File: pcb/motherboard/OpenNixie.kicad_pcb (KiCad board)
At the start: 2 copper layers, 229.9 x 64.9 mm, 141 parts, among them J1 Conn_01x02, J10 Conn_01x10, J2 Conn_01x03, J3 Conn_01x03, J4 DC 12V, J5 Conn_01x04, J6 Conn_01x03, J7 Conn_01x10, J8 Conn_01x10, J9 Conn_01x10, Q1 S8050, Q10 MPSA42, Q11 MPSA42, Q12 MPSA42, Q13 MPSA42, Q14 MPSA42, Q15 MPSA42, Q16 MPSA42, Q17 MPSA42, Q18 MPSA42, Q19 MPSA42, Q2 IRFB4620, Q20 MPSA42, Q21 MPSA42, Q22 MPSA42, Q23 MPSA42, Q24 MPSA42, Q25 MPSA42, Q26 MPSA42, Q27 MPSA42, Q28 MPSA42, Q29 MPSA42, Q3 MPSA42, Q30 MPSA42, Q31 MPSA42, Q32 MPSA42, Q33 MPSA42, Q34 MPSA42, Q35 MPSA42, Q36 MPSA42, Q37 MPSA42, Q38 MPSA42, Q39 MPSA42, Q4 MPSA42, Q40 MPSA42, Q41 MPSA42, Q42 MPSA42, Q5 MPSA42, Q6 MPSA42, Q7 MPSA42, Q8 MPSA42, Q9 MPSA42, SW1 SW_SPST, U1 LM7805_TO220, U10 74LS138, U11 74LS138, U12 74LS138, U13 74LS138, U14 74HC595, U15 74LS138, U16 74LS138, U2 NE555P, U3 MAX1771CSA, U4 DS3231M, U5 24LC16, U6 TSDP341xx, U7 74LS138, U8 74LS138, U9 74HC595

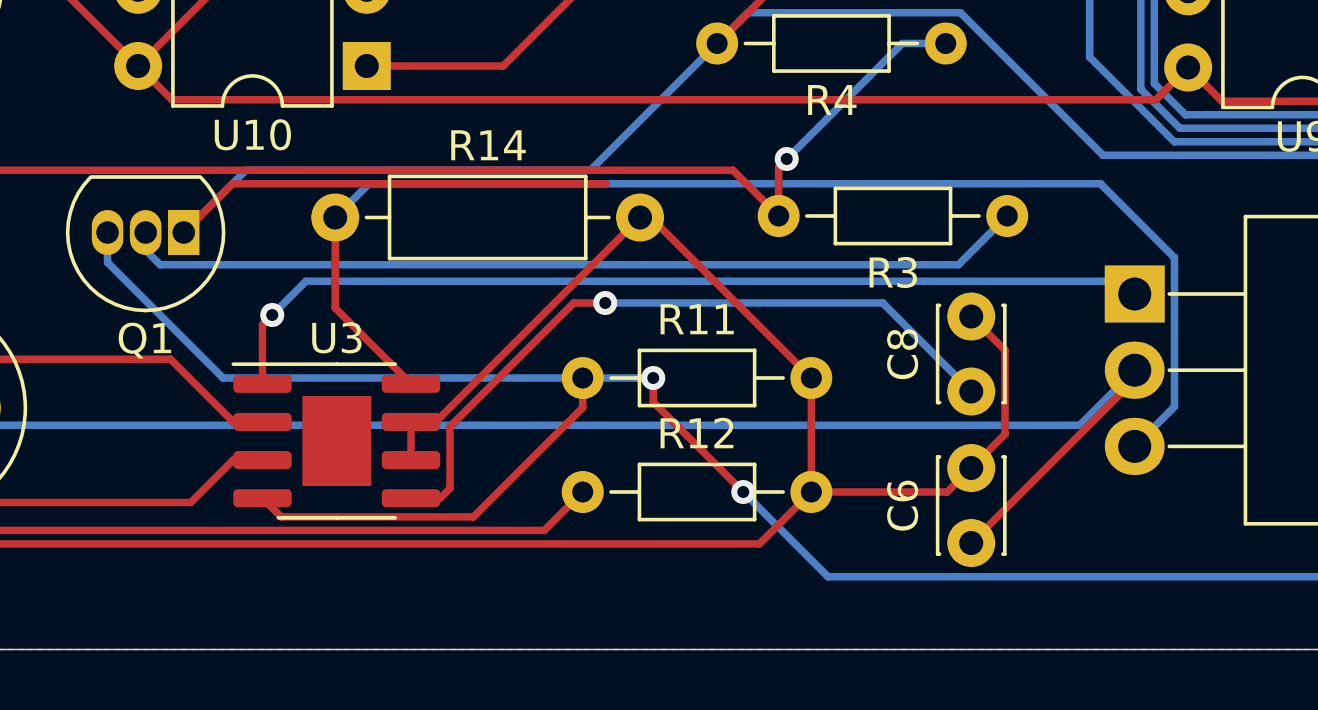
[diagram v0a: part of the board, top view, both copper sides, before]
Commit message: Fix layout errors
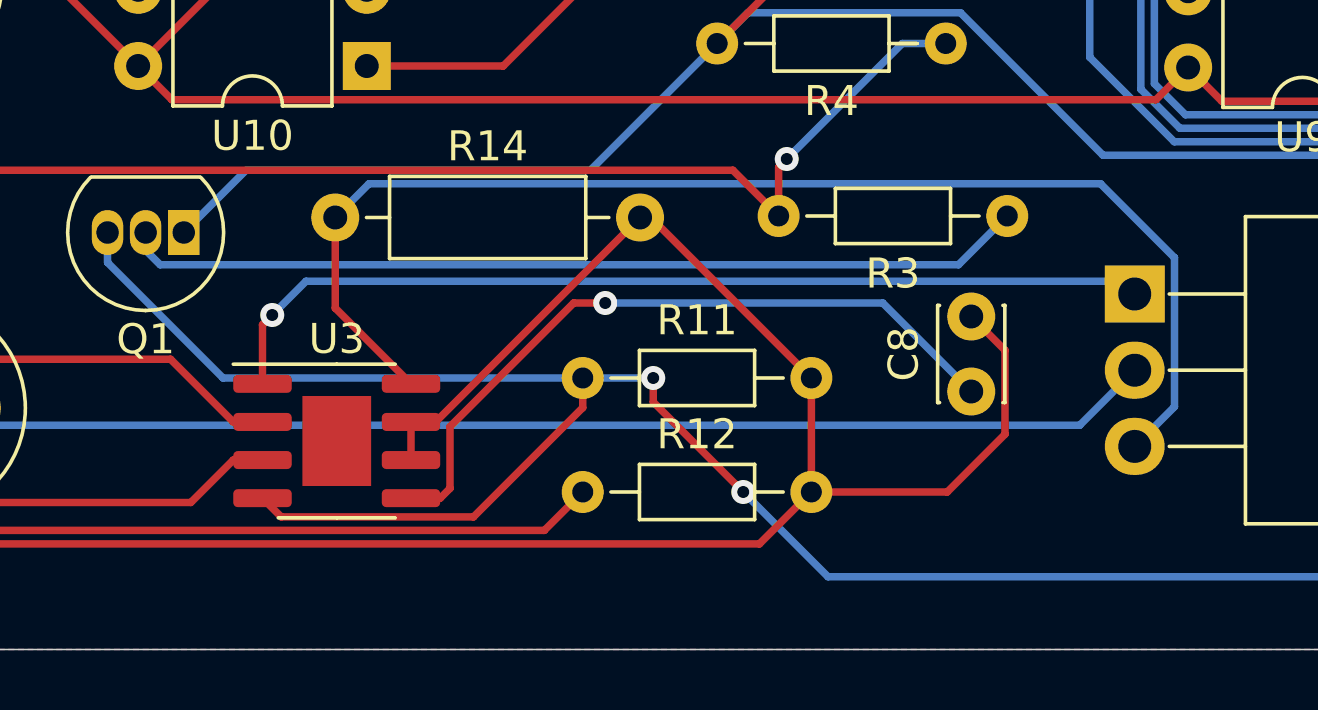
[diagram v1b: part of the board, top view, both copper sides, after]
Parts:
- removed C6: 0.1uF, Capacitor_THT:C_Disc_D3.0mm_W2.0mm_P2.50mm
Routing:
- net GND: track 986.6 -> 971.8 mm
- net Net-(D2-Pad2): track 60.3 -> 52.6 mm

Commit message: Change footprint
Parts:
- C7: footprint Capacitor_THT:CP_Radial_D5.0mm_P2.50mm -> Capacitor_THT:CP_Radial_D8.0mm_P3.80mm
- moved D2 16.2 mm to (142.0, 178.8), turned to 180 degrees
- moved R5 8.36 mm to (126.4, 181.6)
- moved R6 8.36 mm to (126.5, 177.8)
- moved C7 5.69 mm to (112.2, 179.0)
- moved D1 3.35 mm to (118.7, 173.8)
- moved Q1 2.66 mm to (143.3, 172.7)
- moved L1 1.45 mm to (134.7, 177.7), turned to 180 degrees
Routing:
- net GND: track 971.8 -> 933.1 mm
- net Net-(R12-Pad1): track 73.9 -> 58.0 mm
- net Net-(C7-Pad1): track 21.4 -> 36.0 mm
- net BOOST_OUT: track 12.8 -> 21.3 mm
- net Net-(D2-Pad2): track 52.6 -> 57.0 mm
- net Net-(D1-Pad2): track 26.3 -> 22.0 mm
- net Net-(Q1-Pad2): track 30.2 -> 33.0 mm
- net SHDN_PIN: track 92.8 -> 93.4 mm, vias 2 -> 1

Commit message: Fixes
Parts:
- Q2: value IRFB4620 -> TK8P65W; footprint Package_TO_SOT_THT:TO-220-3_Horizontal_TabDown -> Package_TO_SOT_SMD:TO-252-2
- R6: value 20k -> 47k
- moved Q2 9.97 mm to (187.4, 177.3), turned to 0 degrees
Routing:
- net Net-(Q2-Pad3): track 42.9 -> 66.2 mm, vias 0 -> 1
- net Net-(D2-Pad2): track 57.0 -> 68.6 mm, vias 0 -> 1
- net Net-(Q2-Pad1): track 31.8 -> 37.6 mm, vias 1 -> 2

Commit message: Refactoring with 4-bit dynamic scan
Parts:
- removed C1: 10uF, Capacitor_THT:CP_Radial_D5.0mm_P2.50mm
- removed C7: 10uF, Capacitor_THT:CP_Radial_D8.0mm_P3.80mm
- removed C8: 0.1uF, Capacitor_THT:C_Disc_D3.0mm_W2.0mm_P2.50mm
- removed Q18, Q19, Q20, Q21, Q22, Q23, Q24, Q25, Q26, Q27, Q28, Q29, Q30, Q31, Q32, Q33, Q34, Q35, Q36, Q37, Q38, Q39, Q40, Q41, Q42: MPSA42, Package_TO_SOT_THT:TO-92_Inline
- removed R20, R21, R24, R25, R26, R27, R28, R29, R30, R31, R32, R33, R34, R35, R36, R37, R38, R39, R40, R41, R42, R43, R44, R45, R46, R47, R48, R49, R50, R51, R52, R53, R54, R6: 47k, Resistor_THT:R_Axial_DIN0204_L3.6mm_D1.6mm_P7.62mm_Horizontal
- removed R5: 10M, Resistor_THT:R_Axial_DIN0204_L3.6mm_D1.6mm_P7.62mm_Horizontal
- removed REF** (x4): MountingHole_2.1mm, MountingHole:MountingHole_2.1mm
- removed RV1: 200k, Potentiometer_THT:Potentiometer_Vishay_T73YP_Vertical
- removed SW1: SW_SPST, Button_Switch_THT:SW_DIP_SPSTx01_Slide_9.78x4.72mm_W7.62mm_P2.54mm
- removed U11, U12, U13, U15, U16: 74LS138, Package_DIP:DIP-16_W7.62mm
- removed U14: 74HC595, Package_DIP:DIP-16_W7.62mm
- added G1: LOGO, Nixie_Clock:Logo, F.Cu at (166.0, 109.6)
- added J11: Nixie_Conn_12P, Nixie_Clock:Nixie_Conn_12P, F.Cu at (205.9, 96.2)
- added REF1: MountingHole_2.2mm_M2, MountingHole:MountingHole_2.2mm_M2, F.Cu at (77.4, 71.8)
- added REF2: MountingHole_2.2mm_M2, MountingHole:MountingHole_2.2mm_M2, F.Cu at (224.4, 71.8)
- added REF2: MountingHole_2.2mm_M2, MountingHole:MountingHole_2.2mm_M2, F.Cu at (77.4, 121.8)
- added REF3: MountingHole_2.2mm_M2, MountingHole:MountingHole_2.2mm_M2, F.Cu at (224.4, 121.8)
- added locked: 10k, Resistor_THT:R_Axial_DIN0204_L3.6mm_D1.6mm_P2.54mm_Vertical, F.Cu at (127.1, 73.2)
- added locked: 150k, Resistor_THT:R_Axial_DIN0204_L3.6mm_D1.6mm_P2.54mm_Vertical, F.Cu at (127.1, 77.1)
- added locked: 47k, Resistor_THT:R_Axial_DIN0204_L3.6mm_D1.6mm_P2.54mm_Vertical, F.Cu at (107.4, 101.2)
- added locked: 47k, Resistor_THT:R_Axial_DIN0204_L3.6mm_D1.6mm_P2.54mm_Vertical, F.Cu at (135.1, 101.2)
- added locked: 470uF, Capacitor_THT:CP_Radial_D8.0mm_P3.50mm, F.Cu at (107.3, 74.3)
- added locked: 200k, Potentiometer_THT:Potentiometer_Vishay_T73YP_Vertical, F.Cu at (97.0, 73.8)
- BT1: value CR2032 -> 3V; footprint Battery:BatteryHolder_Keystone_1058_1x2032 -> Connector_JST:JST_EH_B2B-EH-A_1x02_P2.50mm_Vertical
- C2: value 1uF -> 10uF; footprint Capacitor_THT:CP_Radial_D5.0mm_P2.50mm -> Capacitor_THT:CP_Radial_D5.0mm_P2.00mm
- C4: value 0.1uF -> 10uF; footprint Capacitor_THT:C_Disc_D3.0mm_W2.0mm_P2.50mm -> Capacitor_THT:CP_Radial_D8.0mm_P3.80mm
- C5: value 470uF -> 0.1uF; footprint Capacitor_THT:CP_Radial_D8.0mm_P3.50mm -> Capacitor_THT:C_Disc_D3.0mm_W2.0mm_P2.50mm
- D1: footprint Diode_THT:D_DO-35_SOD27_P7.62mm_Horizontal -> Diode_THT:D_DO-35_SOD27_P2.54mm_Vertical_AnodeUp
- D3: value LED_RCGB -> LED_RKGB; footprint LED_THT:LED_D5.0mm-4_RGB -> LED_THT:LED_D5.0mm-4_RGB_Wide_Pins
- J10, J8, J9: value Conn_01x10 -> Nixie_Conn_12P; footprint Connector_JST:JST_EH_B10B-EH-A_1x10_P2.50mm_Vertical -> Nixie_Clock:Nixie_Conn_12P
- J2: value Conn_01x03 -> Conn_01x02; footprint Connector_JST:JST_EH_B3B-EH-A_1x03_P2.50mm_Vertical -> Connector_JST:JST_EH_B2B-EH-A_1x02_P2.50mm_Vertical
- J4: value DC 12V -> Nixie_Conn_4P; footprint Connector_BarrelJack:BarrelJack_Horizontal -> Nixie_Clock:Nixie_Conn_4P
- J6: value Conn_01x03 -> 12V; footprint Connector_JST:JST_EH_B3B-EH-A_1x03_P2.50mm_Vertical -> Connector_BarrelJack:BarrelJack_Horizontal
- J7: value Conn_01x10 -> Conn_01x03; footprint Connector_JST:JST_EH_B10B-EH-A_1x10_P2.50mm_Vertical -> Connector_JST:JST_EH_B3B-EH-A_1x03_P2.50mm_Vertical
- Q1: value S8050 -> MPSA42
- Q2: value TK8P65W -> MPSA42; footprint Package_TO_SOT_SMD:TO-252-2 -> Package_TO_SOT_THT:TO-92_Inline
- Q3: value MPSA42 -> TK8P65W; footprint Package_TO_SOT_THT:TO-92_Inline -> Package_TO_SOT_SMD:TO-252-2
- R1, R3: value 1k -> 150k; footprint Resistor_THT:R_Axial_DIN0204_L3.6mm_D1.6mm_P7.62mm_Horizontal -> Resistor_THT:R_Axial_DIN0204_L3.6mm_D1.6mm_P2.54mm_Vertical
- R10, R11, R9: value 4.7k -> 10k; footprint Resistor_THT:R_Axial_DIN0204_L3.6mm_D1.6mm_P7.62mm_Horizontal -> Resistor_THT:R_Axial_DIN0204_L3.6mm_D1.6mm_P2.54mm_Vertical
- R12: value 68k -> 10k; footprint Resistor_THT:R_Axial_DIN0204_L3.6mm_D1.6mm_P7.62mm_Horizontal -> Resistor_THT:R_Axial_DIN0204_L3.6mm_D1.6mm_P2.54mm_Vertical
- R13: value 500 -> 68k; footprint Resistor_THT:R_Axial_DIN0204_L3.6mm_D1.6mm_P7.62mm_Horizontal -> Resistor_THT:R_Axial_DIN0204_L3.6mm_D1.6mm_P2.54mm_Vertical
- R15: value 47k -> 1k; footprint Resistor_THT:R_Axial_DIN0204_L3.6mm_D1.6mm_P7.62mm_Horizontal -> Resistor_THT:R_Axial_DIN0204_L3.6mm_D1.6mm_P2.54mm_Vertical
- R16, R17, R18, R19, R22, R23: footprint Resistor_THT:R_Axial_DIN0204_L3.6mm_D1.6mm_P7.62mm_Horizontal -> Resistor_THT:R_Axial_DIN0204_L3.6mm_D1.6mm_P2.54mm_Vertical
- R2: value 100k -> 1k; footprint Resistor_THT:R_Axial_DIN0204_L3.6mm_D1.6mm_P7.62mm_Horizontal -> Resistor_THT:R_Axial_DIN0204_L3.6mm_D1.6mm_P2.54mm_Vertical
- R4: value 1M -> 10k; footprint Resistor_THT:R_Axial_DIN0204_L3.6mm_D1.6mm_P7.62mm_Horizontal -> Resistor_THT:R_Axial_DIN0204_L3.6mm_D1.6mm_P2.54mm_Vertical
- R7: value 10k -> 150k; footprint Resistor_THT:R_Axial_DIN0204_L3.6mm_D1.6mm_P7.62mm_Horizontal -> Resistor_THT:R_Axial_DIN0204_L3.6mm_D1.6mm_P2.54mm_Vertical
- R8: value 10k -> 10M; footprint Resistor_THT:R_Axial_DIN0204_L3.6mm_D1.6mm_P7.62mm_Horizontal -> Resistor_THT:R_Axial_DIN0204_L3.6mm_D1.6mm_P2.54mm_Vertical
- U10: value 74LS138 -> 74HC04; footprint Package_DIP:DIP-16_W7.62mm -> Package_DIP:DIP-14_W7.62mm
- U3: value MAX1771CSA -> NE555P; footprint Package_SO:SOIC-8-1EP_3.9x4.9mm_P1.27mm_EP2.29x3mm -> Package_DIP:DIP-8_W7.62mm
- U4: value DS3231M -> MAX1771CSA; footprint Package_SO:SOIC-16W_7.5x10.3mm_P1.27mm -> Package_SO:SO-8_3.9x4.9mm_P1.27mm
- U5: value 24LC16 -> DS3231M; footprint Package_DIP:DIP-8_W7.62mm -> Package_SO:SOIC-16W_7.5x10.3mm_P1.27mm
- U6: value TSDP341xx -> 74LS138; footprint OptoDevice:Vishay_MOLD-3Pin -> Package_DIP:DIP-16_W7.62mm
- U7: value 74LS138 -> 74HC595
- U9: value 74HC595 -> 74HC04; footprint Package_DIP:DIP-16_W7.62mm -> Package_DIP:DIP-14_W7.62mm
- moved J2 207.6 mm to (126.0, 85.8), turned to 90 degrees
- moved U6 196.7 mm to (110.4, 113.4), turned to -90 degrees
- moved U5 192.5 mm to (99.9, 83.7), turned to 180 degrees
- moved J6 189.5 mm to (150.9, 83.3), turned to -90 degrees
- moved BT1 165.9 mm to (90.3, 76.0)
- moved J3 162.3 mm to (159.2, 119.5)
- moved U8 160.4 mm to (78.6, 77.7), turned to 0 degrees
- moved R10 150.2 mm to (90.4, 85.7)
- moved R9 144.4 mm to (90.4, 80.7), turned to -90 degrees
- moved R13 143.9 mm to (141.4, 87.5), turned to 0 degrees
- moved R1 136.3 mm to (132.7, 73.2)
- moved U4 133.2 mm to (142.0, 95.8)
- moved Q2 125.0 mm to (115.6, 75.0)
- moved L1 116.7 mm to (193.0, 76.6)
- moved C3 110.5 mm to (200.7, 76.6), turned to 0 degrees
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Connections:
- BT1 pad 1: Net-(BT1-Pad1) -> Net-(#FLG03-pwr)
- C2 pad 1: +12V -> Net-(U2-THR)
- C3 pad 1: Net-(C3-Pad1) -> +12V
- C4 pad 1: +5V -> Net-(D2-K)
- C5 pad 1: +12V -> GND
- C5 pad 2: GND -> Net-(U4-REF)
- D1 pad 1: CONSTANT_PIN -> SHDN_PIN
- D1 pad 2: Net-(D1-Pad2) -> Net-(D1-A)
- D2 pad 1: Net-(C7-Pad1) -> Net-(D2-K)
- D2 pad 2: Net-(D2-Pad2) -> Net-(D2-A)
- D3 pad 1: RED_PIN -> RGB_RED
- D3 pad 2: Net-(D3-Pad2) -> Net-(D3-K)
- D3 pad 3: GREEN_PIN -> RGB_GRN
- D3 pad 4: BLUE_PIN -> RGB_BLE
- J1 pad 1: TIMER_PIN -> I2C_SCL
- J1 pad 2: CONSTANT_PIN -> I2C_SDA
- J10 pad 1: NIXIE_3_P0 -> /NIXIE_Y_P1
- J10 pad 10: NIXIE_3_P9 -> unconnected-(J10-Pad10)
- J10 pad 2: NIXIE_3_P1 -> /NIXIE_Y_P2
- J10 pad 3: NIXIE_3_P2 -> /NIXIE_Y_P3
- J10 pad 4: NIXIE_3_P3 -> /NIXIE_Y_P4
- J10 pad 5: NIXIE_3_P4 -> /NIXIE_Y_P5
- J10 pad 6: NIXIE_3_P5 -> /NIXIE_Y_P6
- J10 pad 7: NIXIE_3_P6 -> /NIXIE_Y_P7
- J10 pad 8: NIXIE_3_P7 -> /NIXIE_Y_P8
- J10 pad 9: NIXIE_3_P8 -> /NIXIE_Y_P9
- J2 pad 1: RED_PIN -> LIGHT_PIN
- J2 pad 2: GREEN_PIN -> SHDN_PIN
- J3 pad 1: LATCH_PIN -> SR_LATCH
- J3 pad 2: DATA_PIN -> SR_DATA
- J3 pad 3: CLOCK_PIN -> SR_CLK
- J5 pad 3: BOOST_OUT -> +170V
- J6 pad 1: I2C_SCL -> +12V
- J6 pad 2: I2C_SDA -> GND
- J6 pad 3: IR_OUT -> unconnected-(J6-Pad3)
- J7 pad 1: NIXIE_0_P0 -> RGB_RED
- J7 pad 2: NIXIE_0_P1 -> RGB_GRN
- J7 pad 3: NIXIE_0_P2 -> RGB_BLE
- J8 pad 1: NIXIE_1_P0 -> /NIXIE_Y_P1
- J8 pad 10: NIXIE_1_P9 -> unconnected-(J8-Pad10)
- J8 pad 2: NIXIE_1_P1 -> /NIXIE_Y_P2
- J8 pad 3: NIXIE_1_P2 -> /NIXIE_Y_P3
- J8 pad 4: NIXIE_1_P3 -> /NIXIE_Y_P4
- J8 pad 5: NIXIE_1_P4 -> /NIXIE_Y_P5
- J8 pad 6: NIXIE_1_P5 -> /NIXIE_Y_P6
- J8 pad 7: NIXIE_1_P6 -> /NIXIE_Y_P7
- J8 pad 8: NIXIE_1_P7 -> /NIXIE_Y_P8
- J8 pad 9: NIXIE_1_P8 -> /NIXIE_Y_P9
- J9 pad 1: NIXIE_2_P0 -> /NIXIE_Y_P1
- J9 pad 10: NIXIE_2_P9 -> unconnected-(J9-Pad10)
- J9 pad 2: NIXIE_2_P1 -> /NIXIE_Y_P2
- J9 pad 3: NIXIE_2_P2 -> /NIXIE_Y_P3
- J9 pad 4: NIXIE_2_P3 -> /NIXIE_Y_P4
- J9 pad 5: NIXIE_2_P4 -> /NIXIE_Y_P5
- J9 pad 6: NIXIE_2_P5 -> /NIXIE_Y_P6
- J9 pad 7: NIXIE_2_P6 -> /NIXIE_Y_P7
- J9 pad 8: NIXIE_2_P7 -> /NIXIE_Y_P8
- J9 pad 9: NIXIE_2_P8 -> /NIXIE_Y_P9
- L1 pad 1: +12V -> Net-(D2-A)
- L1 pad 2: Net-(D2-Pad2) -> +12V
- Q1 pad 2: Net-(Q1-Pad2) -> Net-(Q1-B)
- Q1 pad 3: SHDN_PIN -> Net-(Q1-C)
- Q10 pad 2: Net-(Q10-Pad2) -> /NPN_Y_P2
- Q10 pad 3: NIXIE_1_P2 -> /NIXIE_Y_P2
- Q11 pad 2: Net-(Q11-Pad2) -> /NPN_Y_P3
- Q11 pad 3: NIXIE_0_P5 -> /NIXIE_Y_P3
- Q12 pad 2: Net-(Q12-Pad2) -> /NPN_Y_P4
- Q12 pad 3: NIXIE_1_P5 -> /NIXIE_Y_P4
- Q13 pad 2: Net-(Q13-Pad2) -> /NPN_Y_P5
- Q13 pad 3: NIXIE_0_P4 -> /NIXIE_Y_P5
- Q14 pad 2: Net-(Q14-Pad2) -> /NPN_Y_P6
- Q14 pad 3: NIXIE_1_P4 -> /NIXIE_Y_P6
- Q15 pad 2: Net-(Q15-Pad2) -> /NPN_Y_P7
- Q15 pad 3: NIXIE_0_P7 -> /NIXIE_Y_P7
- Q16 pad 2: Net-(Q16-Pad2) -> /NPN_Y_P8
- Q16 pad 3: NIXIE_1_P7 -> /NIXIE_Y_P8
- Q17 pad 2: Net-(Q17-Pad2) -> /NPN_Y_P9
- Q17 pad 3: NIXIE_0_P6 -> /NIXIE_Y_P9
- Q2 pad 1: Net-(Q2-Pad1) -> GND
- Q2 pad 2: Net-(D2-Pad2) -> Net-(Q2-B)
- Q2 pad 3: Net-(Q2-Pad3) -> Net-(D1-A)
- Q3 pad 1: GND -> Net-(Q3-G)
- Q3 pad 2: Net-(Q3-Pad2) -> Net-(D2-A)
- Q3 pad 3: NIXIE_0_P1 -> Net-(Q3-S)
- Q4 pad 2: Net-(Q4-Pad2) -> Net-(Q4-B)
- Q4 pad 3: NIXIE_1_P1 -> /NIXIE_X_P0
- Q5 pad 2: Net-(Q5-Pad2) -> Net-(Q5-B)
- Q5 pad 3: NIXIE_0_P0 -> /NIXIE_X_P1
- Q6 pad 2: Net-(Q6-Pad2) -> Net-(Q6-B)
- Q6 pad 3: NIXIE_1_P0 -> /NIXIE_X_P2
- Q7 pad 2: Net-(Q7-Pad2) -> Net-(Q7-B)
- Q7 pad 3: NIXIE_0_P3 -> /NIXIE_X_P3
- Q8 pad 2: Net-(Q8-Pad2) -> /NPN_Y_P0
- Q8 pad 3: NIXIE_1_P3 -> /NIXIE_Y_P0
- Q9 pad 2: Net-(Q9-Pad2) -> /NPN_Y_P1
- Q9 pad 3: NIXIE_0_P2 -> /NIXIE_Y_P1
- R1 pad 1: SHDN_PIN -> Net-(D1-A)
- R10 pad 2: I2C_SDA -> I2C_SCL
- R12 pad 1: Net-(R12-Pad1) -> Net-(D2-K)
- R12 pad 2: GND -> +170V
- R13 pad 1: Net-(D3-Pad2) -> GND
- R13 pad 2: GND -> Net-(U4-FB)
- R14 pad 1: Net-(Q2-Pad3) -> GND
- R14 pad 2: GND -> Net-(Q3-S)
- R15 pad 1: Net-(Q3-Pad2) -> GND
- R15 pad 2: /138_0_P1 -> Net-(D3-K)
- R16 pad 1: Net-(Q4-Pad2) -> +170V
- R16 pad 2: /138_1_P1 -> /NIXIE_X_P1
- R17 pad 1: Net-(Q5-Pad2) -> +170V
- R17 pad 2: /138_0_P0 -> /NIXIE_X_P3
- R18 pad 1: Net-(Q6-Pad2) -> +170V
- R18 pad 2: /138_1_P0 -> /NIXIE_X_P0
- R19 pad 1: Net-(Q7-Pad2) -> +170V
- R19 pad 2: /138_0_P3 -> /NIXIE_X_P2
- R2 pad 1: TIMER_PIN -> Net-(U2-DIS)
- R22 pad 1: Net-(Q10-Pad2) -> /NPN_X_P2
- R22 pad 2: /138_1_P2 -> Net-(Q6-B)
- R23 pad 1: Net-(Q11-Pad2) -> /NPN_X_P3
- R23 pad 2: /138_0_P5 -> Net-(Q7-B)
- R3 pad 1: Net-(Q1-Pad2) -> Net-(J4-PadGND)
- R3 pad 2: CONSTANT_PIN -> Net-(Q1-C)
- R4 pad 1: CONSTANT_PIN -> Net-(U2-Q)
- R4 pad 2: GND -> Net-(Q1-B)
- R7 pad 1: +5V -> Net-(U2-THR)
- R7 pad 2: I2C_SDA -> Net-(U2-DIS)
- R8 pad 1: +5V -> Net-(D2-K)
- R8 pad 2: I2C_SCL -> Net-(U4-FB)
- R9 pad 2: I2C_SCL -> I2C_SDA
- U10 pad 1: /595_0_P0 -> /Decoder Inverter/IN_P6
- U10 pad 10: (no net) -> unconnected-(U10-Pad10)
- U10 pad 11: (no net) -> unconnected-(U10-Pad11)
- U10 pad 12: (no net) -> unconnected-(U10-Pad12)
- U10 pad 13: (no net) -> unconnected-(U10-Pad13)
- U10 pad 14: Net-(R29-Pad2) -> +5V
- U10 pad 2: /595_0_P1 -> /NPN_Y_P6
- U10 pad 3: /595_0_P2 -> /Decoder Inverter/IN_P7
- U10 pad 4: GND -> /NPN_Y_P7
- U10 pad 5: GND -> /Decoder Inverter/IN_P8
- U10 pad 6: /595_0_P3 -> /NPN_Y_P8
- U10 pad 7: (no net) -> GND
- U10 pad 8: GND -> /NPN_Y_P9
- U10 pad 9: (no net) -> /Decoder Inverter/IN_P9
- U2 pad 2: TIMER_PIN -> Net-(U2-THR)
- U2 pad 3: Net-(D1-Pad2) -> Net-(U2-Q)
- U2 pad 5: (no net) -> unconnected-(U2-CV-Pad5)
- U2 pad 6: Net-(C3-Pad1) -> Net-(U2-THR)
- U2 pad 7: Net-(C3-Pad1) -> Net-(U2-DIS)
- U3 pad 1: Net-(Q2-Pad1) -> GND
- U3 pad 2: +12V -> LIGHT_PIN
- U3 pad 3: Net-(R12-Pad1) -> Net-(U3-Q)
- U3 pad 4: SHDN_PIN -> +5V
- U3 pad 5: Net-(C8-Pad1) -> unconnected-(U3-CV-Pad5)
- U3 pad 6: GND -> Net-(U3-DIS)
- U3 pad 7: GND -> Net-(U3-DIS)
- U3 pad 8: Net-(Q2-Pad3) -> +5V
- U4 pad 1: (no net) -> Net-(Q3-G)
- U4 pad 2: +5V -> +12V
- U4 pad 3: (no net) -> Net-(U4-FB)
- U4 pad 4: (no net) -> SHDN_PIN
- U4 pad 5: GND -> Net-(U4-REF)
- U4 pad 8: GND -> Net-(Q3-S)
- U5 pad 1: GND -> unconnected-(U5-32KHZ-Pad1)
- U5 pad 2: GND -> +5V
- U5 pad 3: GND -> unconnected-(U5-~{INT}/SQW-Pad3)
- U5 pad 4: GND -> unconnected-(U5-~{RST}-Pad4)
- U5 pad 5: I2C_SDA -> GND
- U5 pad 6: I2C_SCL -> GND
- U5 pad 8: +5V -> GND
- U6 pad 1: IR_OUT -> /DECODER_P0
- U6 pad 2: GND -> /DECODER_P1
- U6 pad 3: +5V -> /DECODER_P2
- U7 pad 1: /595_0_P0 -> /DECODER_P1
- U7 pad 10: /138_0_P5 -> +5V
- U7 pad 11: /138_0_P4 -> SR_CLK
- U7 pad 12: /138_0_P3 -> SR_LATCH
- U7 pad 13: /138_0_P2 -> GND
- U7 pad 14: /138_0_P1 -> SR_DATA
- U7 pad 15: /138_0_P0 -> /DECODER_P0
- U7 pad 2: /595_0_P1 -> /DECODER_P2
- U7 pad 3: /595_0_P2 -> /DECODER_P3
- U7 pad 4: /595_0_P3 -> /NPN_X_P0
- U7 pad 5: GND -> /NPN_X_P1
- U7 pad 6: +5V -> /NPN_X_P2
- U7 pad 7: /138_0_P7 -> /NPN_X_P3
- U7 pad 9: /138_0_P6 -> unconnected-(U7-QH'-Pad9)
- U8 pad 1: /595_0_P4 -> /DECODER_P0
- U8 pad 10: /138_1_P5 -> unconnected-(U8-O5-Pad10)
- U8 pad 11: /138_1_P4 -> unconnected-(U8-O4-Pad11)
- U8 pad 12: /138_1_P3 -> unconnected-(U8-O3-Pad12)
- U8 pad 13: /138_1_P2 -> unconnected-(U8-O2-Pad13)
- U8 pad 14: /138_1_P1 -> /Decoder Inverter/IN_P9
- U8 pad 15: /138_1_P0 -> /Decoder Inverter/IN_P8
- U8 pad 2: /595_0_P5 -> /DECODER_P1
- U8 pad 3: /595_0_P6 -> /DECODER_P2
- U8 pad 4: /595_0_P7 -> GND
- U8 pad 6: +5V -> /DECODER_P3
- U8 pad 7: /138_1_P7 -> unconnected-(U8-O7-Pad7)
- U8 pad 9: /138_1_P6 -> unconnected-(U8-O6-Pad9)
- U9 pad 1: /595_0_P1 -> /Decoder Inverter/IN_P0
- U9 pad 10: +5V -> /NPN_Y_P4
- U9 pad 11: CLOCK_PIN -> /Decoder Inverter/IN_P4
- U9 pad 12: LATCH_PIN -> /NPN_Y_P5
- U9 pad 13: GND -> /Decoder Inverter/IN_P5
- U9 pad 14: DATA_PIN -> +5V
- U9 pad 2: /595_0_P2 -> /NPN_Y_P0
- U9 pad 3: /595_0_P3 -> /Decoder Inverter/IN_P1
- U9 pad 4: /595_0_P4 -> /NPN_Y_P1
- U9 pad 5: /595_0_P5 -> /Decoder Inverter/IN_P2
- U9 pad 6: /595_0_P6 -> /NPN_Y_P2
- U9 pad 7: /595_0_P7 -> GND
- U9 pad 8: GND -> /NPN_Y_P3
- U9 pad 9: CASCADE_PIN -> /Decoder Inverter/IN_P3
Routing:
- net GND: track 933.1 -> 0.00 mm, vias 2 -> 0
- net +5V: track 637.0 -> 300.2 mm
- net +170V: track 0.00 -> 217.3 mm, vias 0 -> 1
- net /NIXIE_Y_P3: track 0.00 -> 182.1 mm
- net /NIXIE_Y_P1: track 0.00 -> 178.1 mm
- net /NIXIE_Y_P5: track 0.00 -> 176.3 mm
- net CLOCK_PIN: track 175.8 -> 0.00 mm, vias 1 -> 0
- net /NIXIE_Y_P2: track 0.00 -> 170.5 mm
- net /NIXIE_Y_P4: track 0.00 -> 169.2 mm
- net /NIXIE_Y_P6: track 0.00 -> 164.8 mm
- net LATCH_PIN: track 160.0 -> 0.00 mm, vias 3 -> 0
- net /NIXIE_Y_P7: track 0.00 -> 158.4 mm
- net /NIXIE_Y_P0: track 0.00 -> 154.3 mm
- net /NIXIE_Y_P9: track 0.00 -> 153.3 mm
- net /NIXIE_Y_P8: track 0.00 -> 152.7 mm
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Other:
- board size 229.9 x 64.9 mm -> 152 x 55 mm
- net class Default removed
- board text added: "OpenNixie@ibcl.us https://github.com/bclswl0827/OpenNixie"

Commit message: Ver 3.0
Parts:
- removed BT1: 3V, Connector_JST:JST_EH_B2B-EH-A_1x02_P2.50mm_Vertical
- removed the J1 at (108.9, 85.9)
- removed the R10 at (90.4, 85.7)
- removed R22, R23: 47k, Resistor_THT:R_Axial_DIN0204_L3.6mm_D1.6mm_P2.54mm_Vertical
- removed the R9 at (90.4, 80.7)
- removed the REF2 at (77.4, 121.8)
- removed the U5 at (99.9, 83.7)
- removed the U9 at (130.4, 113.4)
- removed the locked at (107.4, 101.2)
- removed the locked at (135.1, 101.2)
- added Q10: S8050, Package_TO_SOT_THT:TO-92_Inline, F.Cu at (164.9, 108.9)
- added Q11: S8050, Package_TO_SOT_THT:TO-92_Inline, F.Cu at (158.6, 108.8)
- added Q8: S8050, Package_TO_SOT_THT:TO-92_Inline, F.Cu at (177.2, 108.8)
- added Q9: S8050, Package_TO_SOT_THT:TO-92_Inline, F.Cu at (171.0, 108.9)
- added R18: 47k, Resistor_THT:R_Axial_DIN0204_L3.6mm_D1.6mm_P5.08mm_Horizontal, F.Cu at (138.6, 94.4)
- added R19: 47k, Resistor_THT:R_Axial_DIN0204_L3.6mm_D1.6mm_P5.08mm_Horizontal, F.Cu at (192.8, 94.4)
- added R20: 47k, Resistor_THT:R_Axial_DIN0204_L3.6mm_D1.6mm_P5.08mm_Horizontal, F.Cu at (110.6, 94.4)
- added R21: 47k, Resistor_THT:R_Axial_DIN0204_L3.6mm_D1.6mm_P5.08mm_Horizontal, F.Cu at (165.2, 94.4)
- added REF4: MountingHole_2.2mm_M2, MountingHole:MountingHole_2.2mm_M2, F.Cu at (77.4, 121.8)
- added U8: 74HC04, Package_DIP:DIP-14_W7.62mm, F.Cu at (130.4, 113.4)
- Q2: value MPSA42 -> S8050
- R1: value 150k -> 47k; footprint Resistor_THT:R_Axial_DIN0204_L3.6mm_D1.6mm_P2.54mm_Vertical -> Resistor_THT:R_Axial_DIN0204_L3.6mm_D1.6mm_P5.08mm_Horizontal
- R10: renamed from R12; value 10k -> 6.8k; footprint Resistor_THT:R_Axial_DIN0204_L3.6mm_D1.6mm_P2.54mm_Vertical -> Resistor_THT:R_Axial_DIN0309_L9.0mm_D3.2mm_P12.70mm_Horizontal
- R11: renamed from R13; footprint Resistor_THT:R_Axial_DIN0204_L3.6mm_D1.6mm_P2.54mm_Vertical -> Resistor_THT:R_Axial_DIN0204_L3.6mm_D1.6mm_P5.08mm_Horizontal
- R12: renamed from R15; footprint Resistor_THT:R_Axial_DIN0204_L3.6mm_D1.6mm_P2.54mm_Vertical -> Resistor_THT:R_Axial_DIN0204_L3.6mm_D1.6mm_P5.08mm_Horizontal
- R14: renamed from R16; footprint Resistor_THT:R_Axial_DIN0204_L3.6mm_D1.6mm_P2.54mm_Vertical -> Resistor_THT:R_Axial_DIN0309_L9.0mm_D3.2mm_P12.70mm_Horizontal
- R15: renamed from R17; footprint Resistor_THT:R_Axial_DIN0204_L3.6mm_D1.6mm_P2.54mm_Vertical -> Resistor_THT:R_Axial_DIN0309_L9.0mm_D3.2mm_P12.70mm_Horizontal
- R16: renamed from R18; footprint Resistor_THT:R_Axial_DIN0204_L3.6mm_D1.6mm_P2.54mm_Vertical -> Resistor_THT:R_Axial_DIN0309_L9.0mm_D3.2mm_P12.70mm_Horizontal
- R17: renamed from R19; footprint Resistor_THT:R_Axial_DIN0204_L3.6mm_D1.6mm_P2.54mm_Vertical -> Resistor_THT:R_Axial_DIN0309_L9.0mm_D3.2mm_P12.70mm_Horizontal
- R2, R4, R7, R8, locked (x2): footprint Resistor_THT:R_Axial_DIN0204_L3.6mm_D1.6mm_P2.54mm_Vertical -> Resistor_THT:R_Axial_DIN0204_L3.6mm_D1.6mm_P5.08mm_Horizontal
- R3: value 150k -> 470k; footprint Resistor_THT:R_Axial_DIN0204_L3.6mm_D1.6mm_P2.54mm_Vertical -> Resistor_THT:R_Axial_DIN0204_L3.6mm_D1.6mm_P5.08mm_Horizontal
- R9: renamed from R11; footprint Resistor_THT:R_Axial_DIN0204_L3.6mm_D1.6mm_P2.54mm_Vertical -> Resistor_THT:R_Axial_DIN0204_L3.6mm_D1.6mm_P5.08mm_Horizontal
- moved J2 63.5 mm to (222.0, 110.0), turned to -90 degrees
- moved Q1 61.9 mm to (138.6, 74.8), turned to 0 degrees
- moved C2 53.3 mm to (185.2, 79.8)
- moved R3 46.2 mm to (137.2, 79.9)
- moved R4 40.6 mm to (137.2, 83.4)
- moved D2 36.9 mm to (194.9, 79.7), turned to 90 degrees
- moved R15 31.6 mm to (185.8, 99.9), turned to 0 degrees
- moved R8 30.2 mm to (129.1, 83.4), turned to 0 degrees
- moved Q6 29.8 mm to (158.9, 94.4), turned to 0 degrees
- moved J5 29.4 mm to (222.0, 98.0), turned to -90 degrees
- moved Q7 29.3 mm to (186.7, 94.4), turned to 0 degrees
- moved R1 28.4 mm to (107.0, 85.3)
- moved J4 26.6 mm to (114.0, 72.6), turned to 0 degrees
- moved J1 26.5 mm to (103.0, 72.6), turned to 0 degrees
- moved R9 25.7 mm to (107.0, 78.2)
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- renumbered J2 to J1, J11 to J10, J3 to J2, J4 to J3, J5 to J4, J7 to J5, J8 to J7, J9 to J8, J10 to J9, Q8 to Q12, Q9 to Q13, Q10 to Q14, Q11 to Q15, Q12 to Q16, Q13 to Q17, Q14 to Q18, Q15 to Q19, Q16 to Q20, Q17 to Q21, R14 to R13, U6 to U5, U7 to U6, U8 to U7, U10 to U9
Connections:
- net /NPN_Y_P6 renamed /NOT_Y_P6
- net /NPN_Y_P7 renamed /NOT_Y_P7
- net /NPN_Y_P8 renamed /NOT_Y_P8
- net /NPN_Y_P9 renamed /NOT_Y_P9
- C5 pad 1: GND -> Net-(U4-REF)
- C5 pad 2: Net-(U4-REF) -> GND
- J2 pad 1: SR_LATCH -> SR_CLK
- J2 pad 3: SR_CLK -> SR_LATCH
- J4 pad 2: +12V -> +170V
- J4 pad 3: +170V -> +12V
- Q12 pad 2: /NPN_Y_P0 -> /NOT_Y_P0
- Q13 pad 2: /NPN_Y_P1 -> /NOT_Y_P1
- Q14 pad 2: /NPN_Y_P2 -> /NOT_Y_P2
- Q15 pad 2: /NPN_Y_P3 -> /NOT_Y_P3
- Q16 pad 2: /NPN_Y_P4 -> /NOT_Y_P4
- Q17 pad 2: /NPN_Y_P5 -> /NOT_Y_P5
- R10 pad 1: Net-(D2-K) -> +170V
- R10 pad 2: +170V -> Net-(D2-K)
- R11 pad 1: GND -> Net-(U4-FB)
- R11 pad 2: Net-(U4-FB) -> GND
- R15 pad 1: +170V -> /NIXIE_X_P3
- R15 pad 2: /NIXIE_X_P3 -> +170V
- R2 pad 2: +5V -> +12V
- R8 pad 1: Net-(D2-K) -> Net-(U4-FB)
- R8 pad 2: Net-(U4-FB) -> Net-(D2-K)
- R9 pad 1: SHDN_PIN -> GND
- R9 pad 2: GND -> SHDN_PIN
- U2 pad 4: +5V -> +12V
- U2 pad 8: +5V -> +12V
- U6 pad 4: /NPN_X_P0 -> /NOT_X_P0
- U6 pad 5: /NPN_X_P1 -> /NOT_X_P1
- U6 pad 6: /NPN_X_P2 -> /NOT_X_P2
- U6 pad 7: /NPN_X_P3 -> /NOT_X_P3
- locked pad 1: Net-(U3-Q) -> Net-(Q2-B)
- locked pad 2: Net-(Q2-B) -> Net-(U3-Q)
- locked pad 1: LIGHT_PIN -> +5V
- locked pad 2: +5V -> LIGHT_PIN
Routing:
- net /NPN_X_P0: track 104.6 -> 0.00 mm
- net /NPN_X_P3: track 89.3 -> 0.00 mm
- net +170V: track 217.3 -> 136.6 mm, vias 1 -> 0
- net +5V: track 300.2 -> 378.1 mm
- net Net-(Q4-B): track 10.4 -> 84.2 mm, vias 0 -> 1
- net +12V: track 92.2 -> 152.9 mm
- net /NPN_X_P2: track 59.4 -> 0.00 mm, vias 1 -> 0
- net SR_DATA: track 15.6 -> 74.0 mm
- net /NPN_Y_P3: track 57.5 -> 0.00 mm
- net /NPN_Y_P4: track 47.1 -> 0.00 mm
- net SR_CLK: track 26.0 -> 71.2 mm
- net SR_LATCH: track 17.3 -> 60.9 mm
- net /NOT_Y_P4: track 0.00 -> 39.0 mm, vias 0 -> 2
- net /NIXIE_Y_P2: track 170.5 -> 208.8 mm
- net /DECODER_P0: track 119.9 -> 157.9 mm, vias 1 -> 0
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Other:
- board text added: "locked"
- board text removed: "OpenNixie@ibcl.us https://github.com/bclswl0827/OpenNixie"

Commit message: Update resistor value
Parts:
- R10: value 6.8k -> 1k
- R14, R15, R16, R17, R18, R19, R20, R21: value 47k -> 36k
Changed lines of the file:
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@@
         (effects (font (size 1 1) (thickness 0.15)))
     )
-    (fp_text value "6.8k" (at 6.35 2.72) (layer "F.Fab")
+    (fp_text value "1k" (at 6.35 2.72) (layer "F.Fab")
         (effects (font (size 1 1) (thickness 0.15)))
     )
@@
         (effects (font (size 1 1) (thickness 0.15)))
     )
-    (fp_text value "47k" (at 6.35 2.72 180) (layer "F.Fab")
+    (fp_text value "36k" (at 6.35 2.72 180) (layer "F.Fab")
         (effects (font (size 1 1) (thickness 0.15)))
     )
@@
         (effects (font (size 1 1) (thickness 0.15)))
     )
-    (fp_text value "47k" (at 6.35 2.72) (layer "F.Fab")
+    (fp_text value "36k" (at 6.35 2.72) (layer "F.Fab")
         (effects (font (size 1 1) (thickness 0.15)))
     )
@@
         (effects (font (size 1 1) (thickness 0.15)))
     )
-    (fp_text value "47k" (at 6.35 2.72 180) (layer "F.Fab")
+    (fp_text value "36k" (at 6.35 2.72 180) (layer "F.Fab")
         (effects (font (size 1 1) (thickness 0.15)))
     )
@@
         (effects (font (size 1 1) (thickness 0.15)))
     )
-    (fp_text value "47k" (at 6.35 2.72 180) (layer "F.Fab")
+    (fp_text value "36k" (at 6.35 2.72 180) (layer "F.Fab")
         (effects (font (size 1 1) (thickness 0.15)))
     )
@@
         (effects (font (size 1 1) (thickness 0.15)))
     )
-    (fp_text value "47k" (at 2.54 1.92) (layer "F.Fab")
+    (fp_text value "36k" (at 2.54 1.92) (layer "F.Fab")
         (effects (font (size 1 1) (thickness 0.15)))
     )
@@
         (effects (font (size 1 1) (thickness 0.15)))
     )
-    (fp_text value "47k" (at 2.54 1.92) (layer "F.Fab")
+    (fp_text value "36k" (at 2.54 1.92) (layer "F.Fab")
         (effects (font (size 1 1) (thickness 0.15)))
     )
@@
         (effects (font (size 1 1) (thickness 0.15)))
     )
-    (fp_text value "47k" (at 2.54 1.92) (layer "F.Fab")
+    (fp_text value "36k" (at 2.54 1.92) (layer "F.Fab")
         (effects (font (size 1 1) (thickness 0.15)))
     )
@@
         (effects (font (size 1 1) (thickness 0.15)))
     )
-    (fp_text value "47k" (at 2.54 1.92) (layer "F.Fab")
+    (fp_text value "36k" (at 2.54 1.92) (layer "F.Fab")
         (effects (font (size 1 1) (thickness 0.15)))
     )
